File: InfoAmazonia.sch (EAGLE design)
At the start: 51 parts, among them IC1 CA3140AM Z, IC2 TL081BCDG4, IC3 TL032C, IC4 LM2662, IC5 ADAFRUIT_FONA, IC6 SHT20, IC7 MIC29302AWD, IC8 4050D, J1 BNCPTH, J2 BNCPTH, U1 ARDUINO-MEGAPRO, U2 MPL3115A2, U3 USD-SOCKETNEW

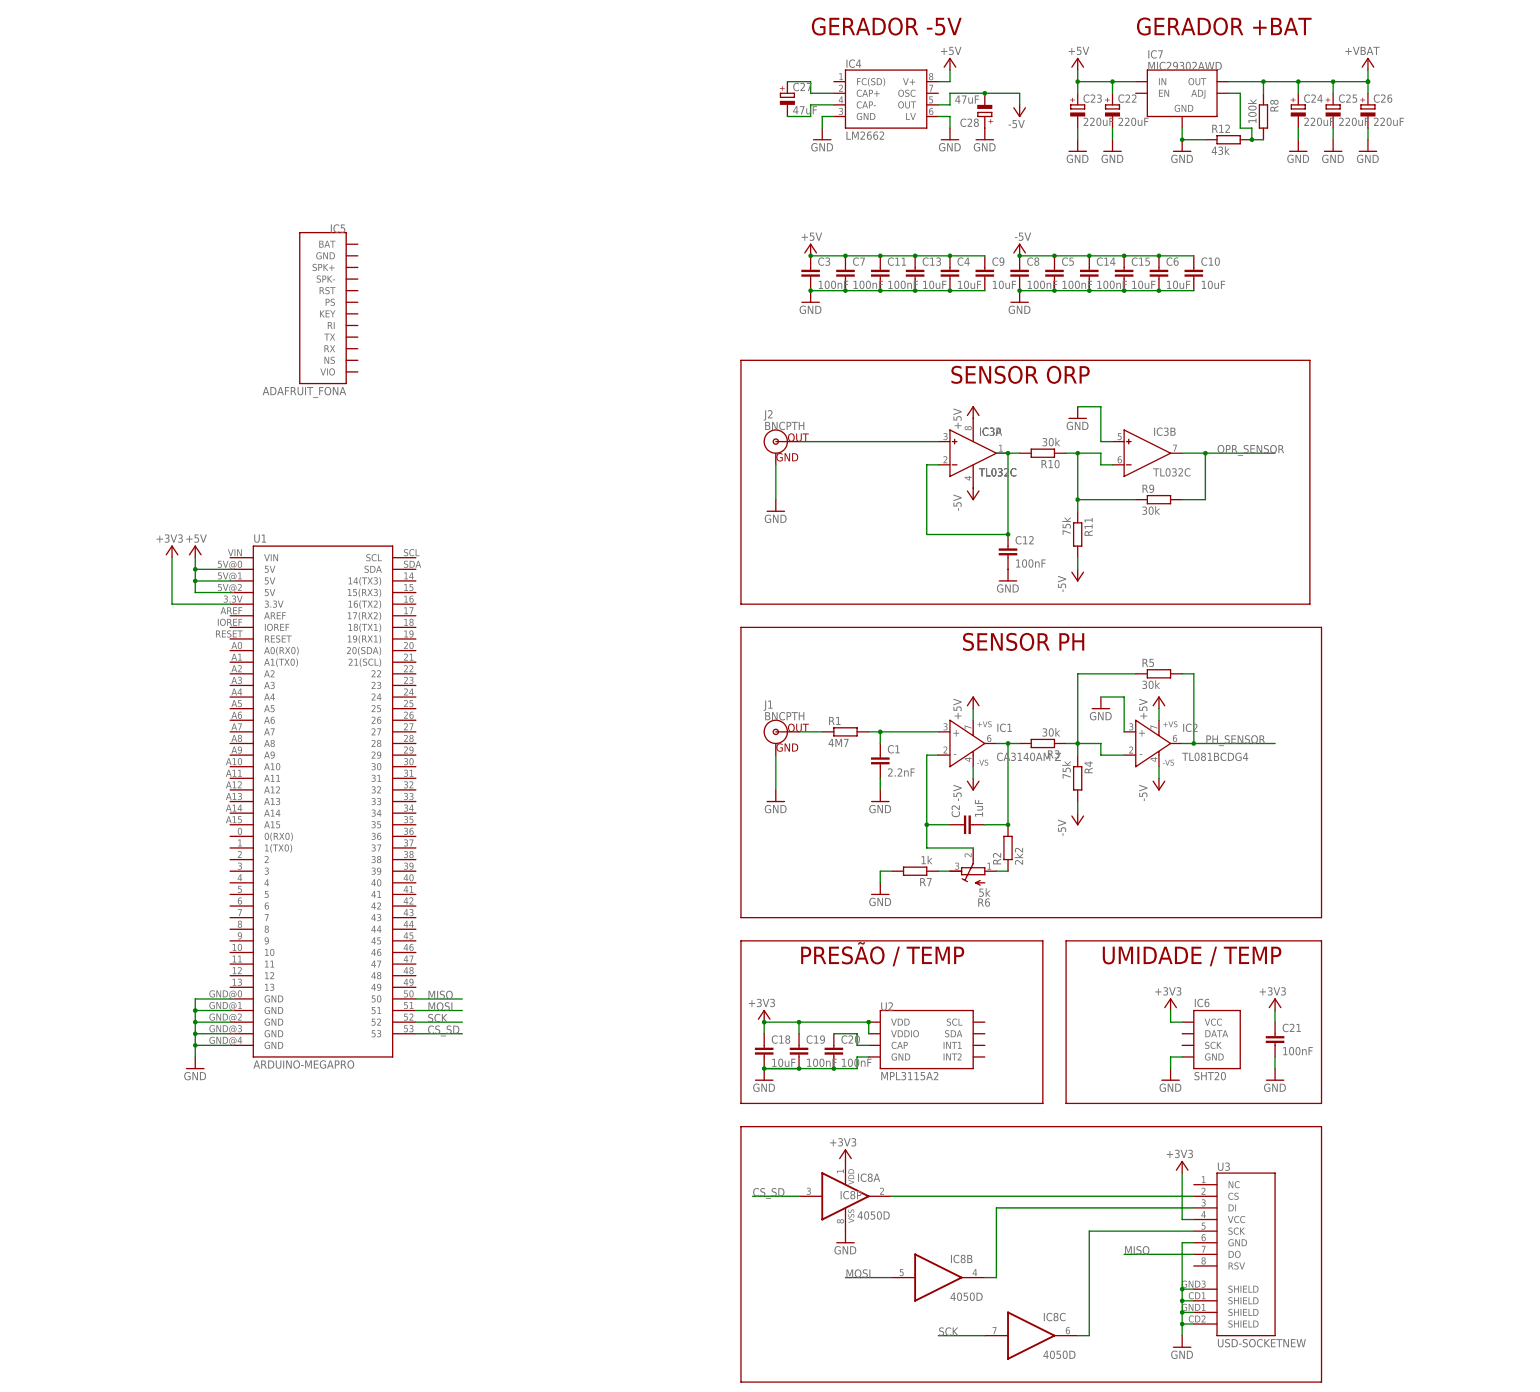
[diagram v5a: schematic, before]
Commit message: - Decidido que sera utilizado o sensor do rifle pra EC
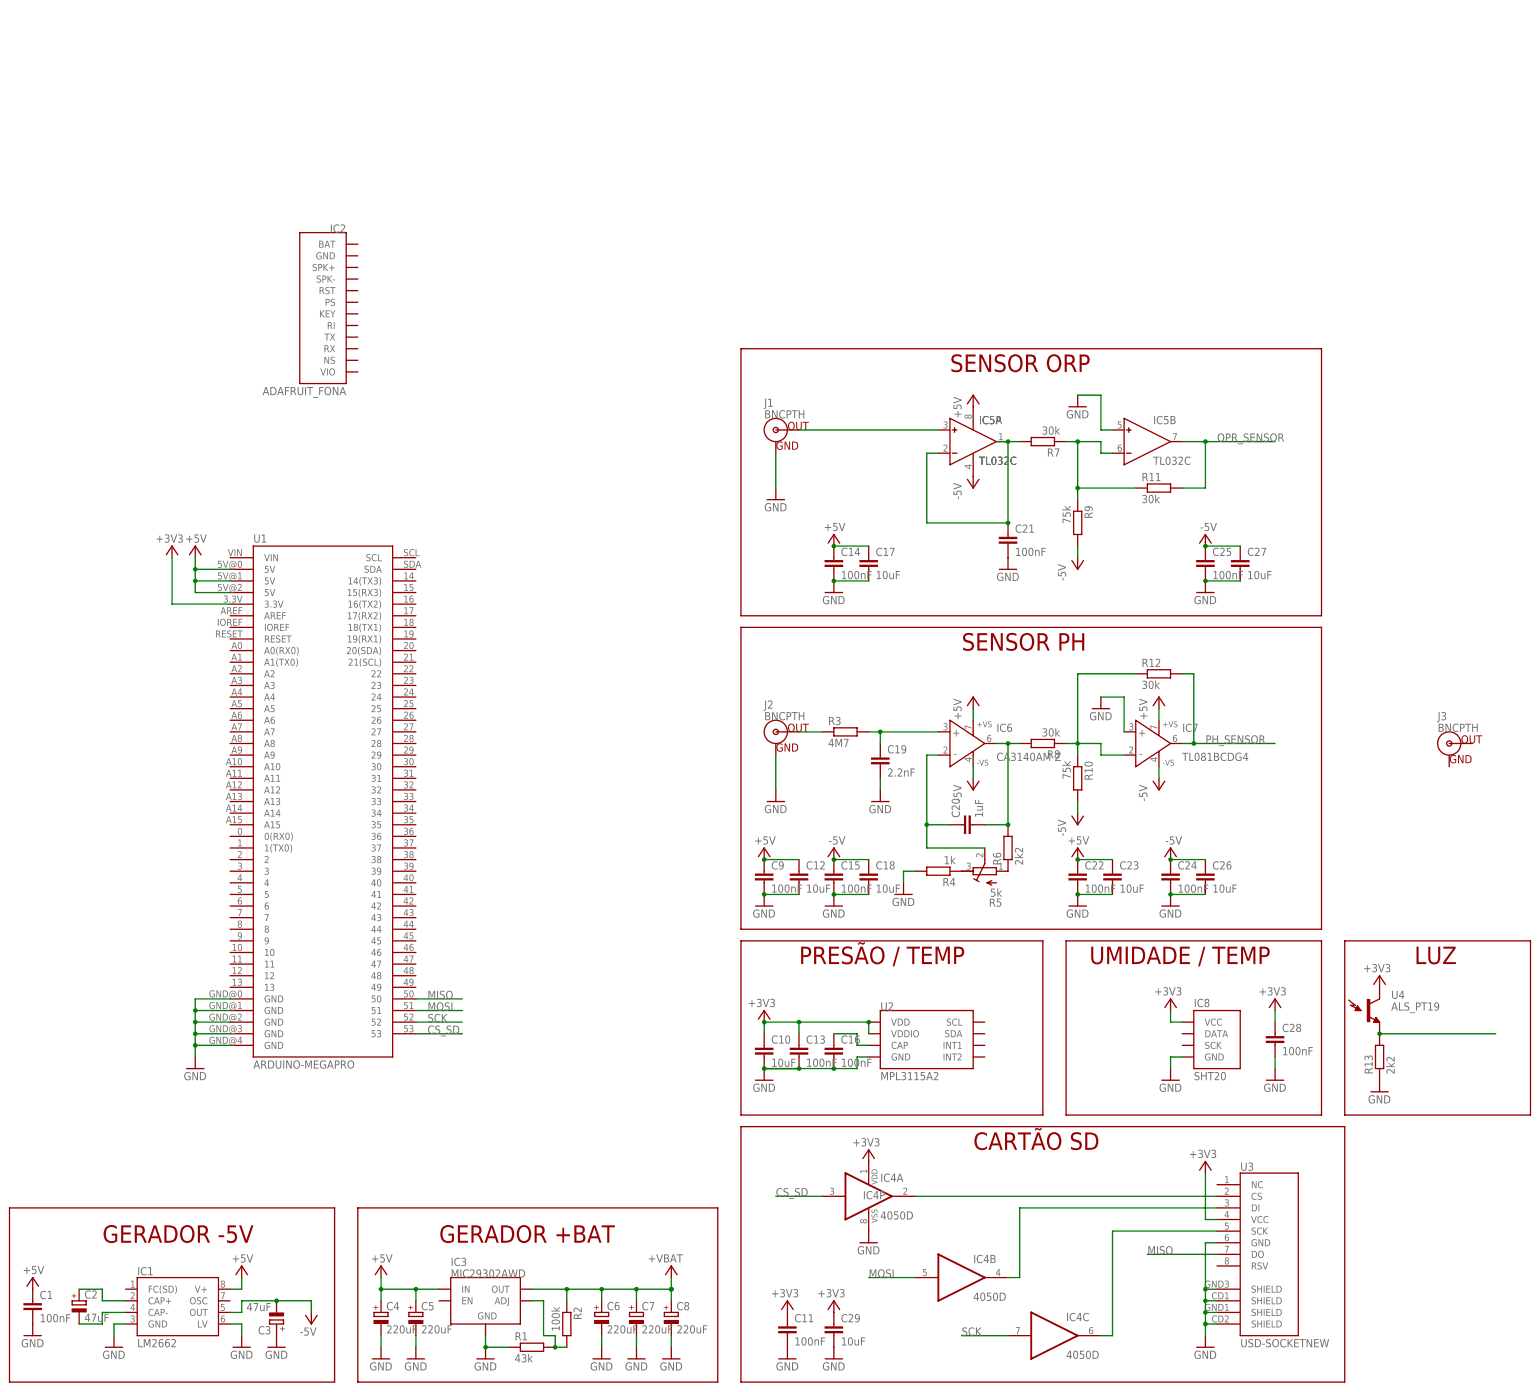
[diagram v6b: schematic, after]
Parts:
- added C16: 100nF, InfoAmazonia:C-EUC0603
- added C17, C29: 10uF, InfoAmazonia:C-EUC0603
- added J3: BNCPTH, InfoAmazonia:BNCPTH
- added R13: 2k2, InfoAmazonia:R-EU_R0603
- added U4: ALS_PT19, InfoAmazonia:LIGHTSENSORALS
- C1: value 2.2nF -> 100nF
- C12: value 100nF -> 10uF
- C13, C15, C9: value 10uF -> 100nF
- C19: value 100nF -> 2.2nF
- C2: value 1uF -> 47uF; device InfoAmazonia:C-EUC0603 -> InfoAmazonia:CPOL-EUSMC_B
- C20: value 100nF -> 1uF
- C22, C24, C25: value 220uF -> 100nF; device InfoAmazonia:CPOL-EUUD6,3-5,8 -> InfoAmazonia:C-EUC0603
- C23, C26: value 220uF -> 10uF; device InfoAmazonia:CPOL-EUUD6,3-5,8 -> InfoAmazonia:C-EUC0603
- C27: value 47uF -> 10uF; device InfoAmazonia:CPOL-EUSMC_B -> InfoAmazonia:C-EUC0603
- C28: value 47uF -> 100nF; device InfoAmazonia:CPOL-EUSMC_B -> InfoAmazonia:C-EUC0603
- C3: value 100nF -> 47uF; device InfoAmazonia:C-EUC0603 -> InfoAmazonia:CPOL-EUSMC_B
- C4, C6: value 10uF -> 220uF; device InfoAmazonia:C-EUC0603 -> InfoAmazonia:CPOL-EUUD6,3-5,8
- C5, C7, C8: value 100nF -> 220uF; device InfoAmazonia:C-EUC0603 -> InfoAmazonia:CPOL-EUUD6,3-5,8
- IC1: value CA3140AM Z -> LM2662; device InfoAmazonia:AMPOP -> InfoAmazonia:LM2662
- IC2: value TL081BCDG4 -> ADAFRUIT_FONA; device InfoAmazonia:AMPOP -> InfoAmazonia:ADAFRUIT_FONA
- IC3: value TL032C -> MIC29302AWD; device InfoAmazonia:AMPOP_2R -> InfoAmazonia:MIC29XXX
- IC4: value LM2662 -> 4050D; device InfoAmazonia:LM2662 -> InfoAmazonia:4050D
- IC5: value ADAFRUIT_FONA -> TL032C; device InfoAmazonia:ADAFRUIT_FONA -> InfoAmazonia:AMPOP_2R
- IC6: value SHT20 -> CA3140AM Z; device InfoAmazonia:SHT2X -> InfoAmazonia:AMPOP
- IC7: value MIC29302AWD -> TL081BCDG4; device InfoAmazonia:MIC29XXX -> InfoAmazonia:AMPOP
- IC8: value 4050D -> SHT20; device InfoAmazonia:4050D -> InfoAmazonia:SHT2X
- R1: value 4M7 -> 43k
- R10, R9: value 30k -> 75k
- R11: value 75k -> 30k
- R12: value 43k -> 30k
- R2: value 2k2 -> 100k
- R3: value 30k -> 4M7
- R4: value 75k -> 1k
- R5: value 30k -> 5k; device InfoAmazonia:R-EU_R0603 -> InfoAmazonia:RTRIM329W
- R6: value 5k -> 2k2; device InfoAmazonia:RTRIM329P -> InfoAmazonia:R-EU_R0603
- R7: value 1k -> 30k
- R8: value 100k -> 30k
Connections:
- removed net N$10: C6.2
- removed net N$11: C6.1
- removed net N$12: C5.1
- net +3V3: now also C10.1, C11.1, C13.1, C28.1, C29.1, IC4P.VDD, IC8.VCC, U4.C1; no longer C18.1, C19.1, C21.1, IC6.VCC, IC8P.VDD
- net +5V: now also C1.1, C12.1, C14.1, C17.1, C22.1, C23.1, C4.+, C5.+, IC1.V+, IC3.IN, IC5P.V+, IC6.+VS, IC7.+VS; no longer C11.1, C13.1, C22.+, C23.+, C3.1, C4.1, C7.1, IC1.+VS, IC2.+VS, IC3P.V+, IC4.V+, IC7.IN
- net +VBAT: now also C6.+, C7.+, C8.+, IC3.OUT, R2.1; no longer C24.+, C25.+, C26.+, IC7.OUT, R8.1
- net -5V: now also C18.1, C24.1, C25.1, C26.1, C27.1, C3.-, IC1.OUT, IC5P.V-, IC6.-VS, IC7.-VS, R10.2, R9.2; no longer C10.1, C14.1, C28.-, C8.1, IC1.-VS, IC2.-VS, IC3P.V-, IC4.OUT, R11.2, R4.2
- net CS_SD: now also IC4A.I; no longer IC8A.I
- net GND: now also C16.2, C17.2, C22.2, C23.2, C24.2, C25.2, C26.2, C27.2, C28.2, C29.2, C3.+, C4.-, C5.-, C6.-, C7.-, C8.-, IC1.GND, IC1.LV, IC3.GND, IC4P.VSS, IC5B.IN+, IC7.IN+, IC8.GND, R1.1, R13.1, R4.2; no longer C20.2, C22.-, C23.-, C24.-, C25.-, C26.-, C28.+, C3.2, C4.2, C7.2, C8.2, IC2.IN+, IC3B.IN+, IC4.GND, IC4.LV, IC6.GND, IC7.GND, IC8P.VSS, R12.1, R7.2
- net MOSI: now also IC4B.I; no longer IC8B.I
- net N$1: now also J2.OUT, R3.1; no longer J1.OUT, R1.1
- net N$13: now also IC5A.IN+, J1.OUT; no longer IC3A.IN+, J2.OUT
- net N$14: now also C2.-, IC1.CAP-; no longer C27.-, IC4.CAP-
- net N$15: now also C21.1, IC5A.IN-, IC5A.OUT, R7.2; no longer C12.1, IC3A.IN-, IC3A.OUT, R10.2
- net N$16: now also C2.+, IC1.CAP+; no longer C27.+, IC4.CAP+
- net N$17: now also IC5B.IN-, R7.1; no longer IC3B.IN-, R10.1
- net N$18: now also IC3.ADJ, R1.2, R2.2; no longer IC7.ADJ, R12.2, R8.2
- net N$19: now also IC4C.O; no longer IC8C.O
- net N$2: now also C19.1, IC6.IN+, R3.2; no longer C1.1, IC1.IN+, R1.2
- net N$20: now also IC4B.O; no longer IC8B.O
- net N$21: now also IC4A.O; no longer IC8A.O
- net N$3: now also C20.1, IC6.IN-, R5.S; no longer C2.1, IC1.IN-, R6.S
- net N$4: now also C20.2, IC6.OUT, R6.2, R8.2; no longer C2.2, IC1.OUT, R2.2, R3.2
- net N$5: now also IC7.IN-, R10.1, R12.1, R8.1; no longer IC2.IN-, R3.1, R4.1, R5.1
- net N$6: now also R4.1, R5.E; no longer R6.E, R7.1
- net N$7: now also C16.1; no longer C20.1
- net N$8: now also R5.A, R6.1; no longer R2.1, R6.A
- net N$9: now also R13.2, U4.E1; no longer C5.2
- net OPR_SENSOR: now also IC5B.OUT, R11.2; no longer IC3B.OUT, R9.2
- net PH_SENSOR: now also IC7.OUT, R12.2; no longer IC2.OUT, R5.2
- net SCK: now also IC4C.I; no longer IC8C.I
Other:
- note added: "CARTÃO SD"
- note added: "LUZ"
- moved on the sheet: C1, C10, C11, C12, C13, C14, C15, C18, C19, C20, C21, C9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

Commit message: - Adicionado sensor de EC
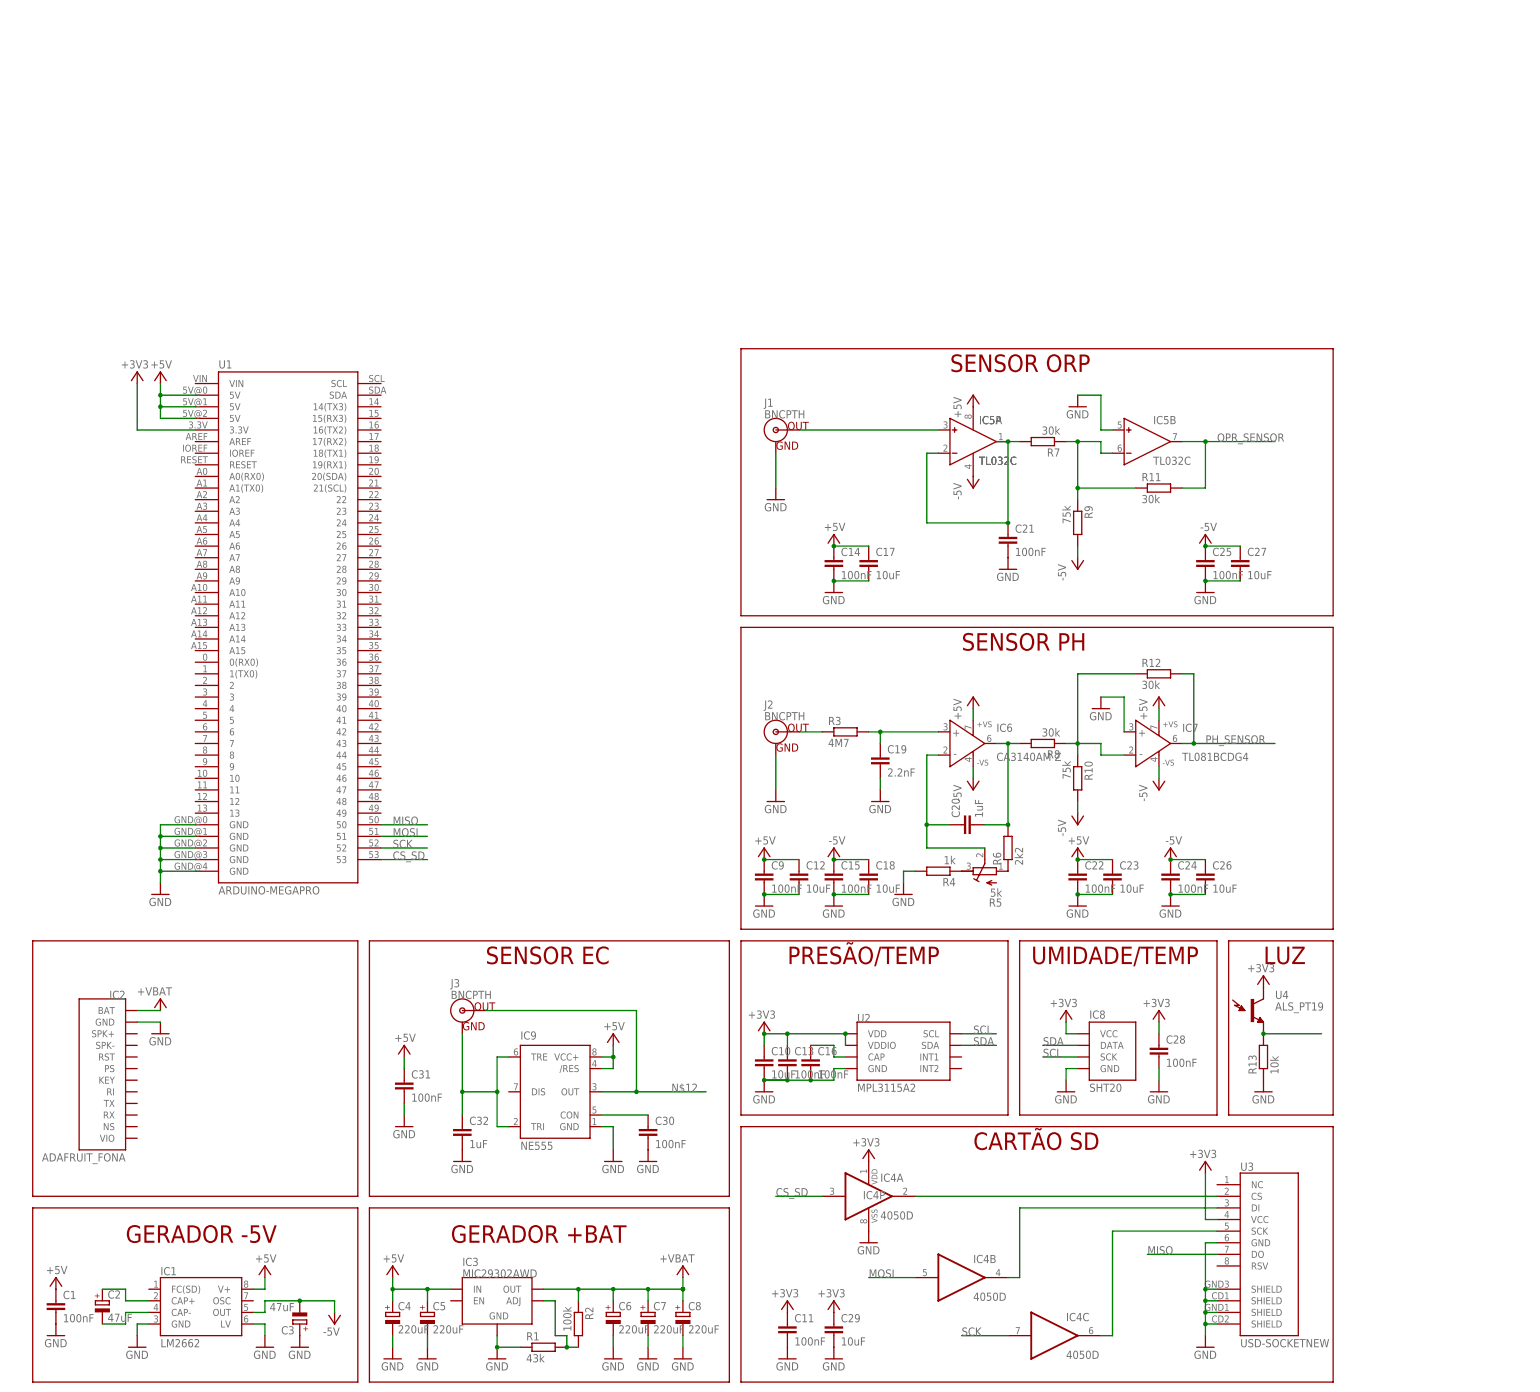
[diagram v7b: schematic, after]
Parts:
- added C30, C31: 100nF, InfoAmazonia:C-EUC0603
- added C32: 1uF, InfoAmazonia:C-EUC0603
- added IC9: NE555, InfoAmazonia:NE555
- R13: value 2k2 -> 10k
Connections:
- new net N$10: C30.1, IC9.CON
- new net N$11: C32.1, IC9.TRE, IC9.TRI, J3.GND
- new net N$12: IC9.OUT, J3.OUT
- new net SCL: IC8.SCK, U2.SCL
- new net SDA: IC8.DATA, U2.SDA
- net +5V: now also C31.1, IC9./RES, IC9.VCC+
- net +VBAT: now also IC2.BAT
- net GND: now also C30.2, C31.2, C32.2, IC2.GND, IC9.GND
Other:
- note added: "PRESÃO/TEMP"
- note added: "SENSOR EC"
- note added: "UMIDADE/TEMP"
- note removed: "PRESÃO / TEMP"
- note removed: "UMIDADE / TEMP"
- moved on the sheet: C1, C10, C13, C16, C2, C28, C3, C4, C5, C6, C7, C8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

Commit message: - Terminado o esquematico
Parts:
- added JP1, JP10, JP11, JP12, JP13, JP2, JP3, JP4, JP5, JP6, JP7, JP8, JP9: (no value), InfoAmazonia:PINHD-1X3180
- added R14, R15, R16: 0, InfoAmazonia:R-EU_R0603
- added R17: 4k7, InfoAmazonia:R-EU_R0603
- IC2: value ADAFRUIT_FONA -> ADAFRUIT FONA
- U4: value ALS_PT19 -> ALS-PT19
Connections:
- removed net OPR_SENSOR: IC5B.OUT, R11.2
- new net 1_SENSOR: JP10.1, R16.2, U1.A2
- new net 2_SENSOR: JP11.1, R15.2, U1.A3
- new net 3_SENSOR: JP12.1, R14.2, U1.A4
- new net EC_IN: C32.1, IC9.TRE, IC9.TRI, JP4.3
- new net EC_SENSOR: IC9.OUT, JP3.1, JP4.2
- new net EN_BAT: IC3.EN, U1.13
- new net FREQ_SENSOR: R14.1, R15.1, R16.1, U1.49
- new net GSM_KEY: IC2.KEY, U1.10
- new net GSM_NS: IC2.NS, U1.7
- new net GSM_PT: IC2.PS, U1.11
- new net GSM_RI: IC2.RI, U1.2
- new net GSM_RST: IC2.RST, U1.12
- new net GSM_RX: IC2.RX, U1.8
- new net GSM_TX: IC2.TX, U1.9
- new net INT1: U1.18(TX1), U2.INT1
- new net INT2: U1.19(RX1), U2.INT2
- new net LUZ_SENSOR: R13.2, U1.A5, U4.E1
- new net N$22: J3.GND, JP5.2
- new net ORP_IN: IC5A.IN+, JP8.3
- new net ORP_SENSOR: IC5B.OUT, JP7.1, R11.2
- new net PH_IN: JP2.3, R3.1
- new net TEMP_SENSOR: JP13.2, R17.2, U1.A6
- net +5V: now also IC2.VIO, JP1.3, JP10.3, JP11.3, JP12.3, JP13.1, JP3.3, JP7.3, R17.1
- net -5V: now also JP1.2, JP10.2, JP11.2, JP12.2, JP3.2, JP7.2
- net GND: now also JP13.3, JP2.1, JP2.2, JP4.1, JP5.1, JP6.1, JP8.1, JP8.2, JP9.1; no longer J1.GND, J2.GND
- net N$1: now also J1.OUT, JP9.3; no longer J2.OUT, R3.1
- net N$11: now also J2.OUT, JP6.3; no longer C32.1, IC9.TRE, IC9.TRI, J3.GND
- net N$12: now also J2.GND, JP6.2; no longer IC9.OUT, J3.OUT
- net N$13: now also J3.OUT, JP5.3; no longer IC5A.IN+, J1.OUT
- net N$9: now also J1.GND, JP9.2; no longer R13.2, U4.E1
- net PH_SENSOR: now also JP1.1
- net SCL: now also U1.SCL
- net SDA: now also U1.SDA
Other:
- note added: "2x"
- note added: "3x"
- note added: "ADAFRUIT FONA"
- note added: "GSM MODULE"
- note added: "SENSOR TEMP"
- moved on the sheet: C10, C11, C13, C14, C16, C17, C21, C22, C23, C24, C26, C28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
